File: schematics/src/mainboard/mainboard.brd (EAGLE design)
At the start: 58.4 x 99.1 mm, 65 parts, among them IC1 LM324N, IC2 7805T, IC3 UA741P, IC6 LM324N, IC8 CA3080E, Q1 BC550C, Q2 BC550C, Q3 BC550C

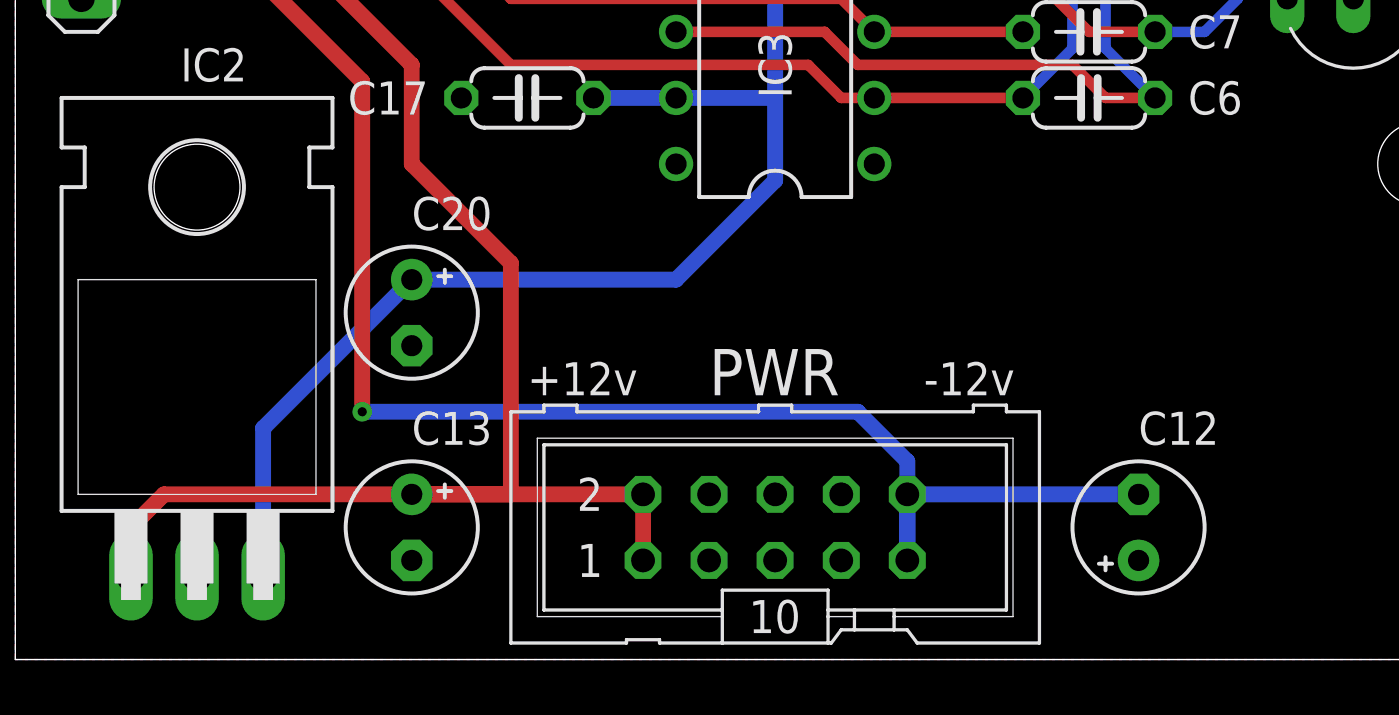
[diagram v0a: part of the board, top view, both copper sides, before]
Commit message: Updated Schematics, Fixed Power Socket orientation
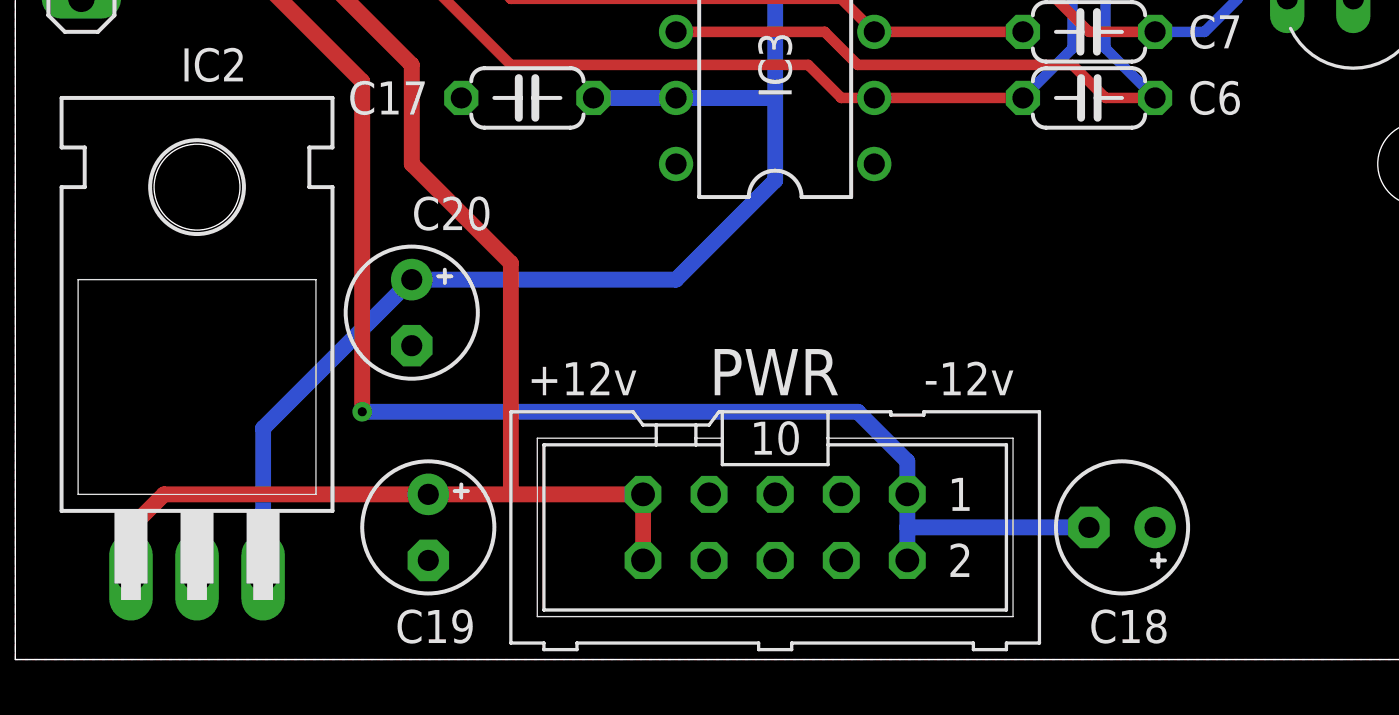
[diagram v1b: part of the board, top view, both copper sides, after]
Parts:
- removed C12, C13: 10uf, resistor:E2,5-5
- added C18, C19: 10uf, resistor:E2,5-5
- turned PWR to 180 degrees
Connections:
- net +12V: now also C19.+, PWR.10, PWR.9; no longer C13.+, PWR.1, PWR.2
- net -12V: now also C18.-, PWR.1, PWR.2; no longer C12.-, PWR.10, PWR.9
- net GND: now also C18.+, C19.-; no longer C12.+, C13.-
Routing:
- net -12V: track 62.8 -> 58.4 mm
- net +12V: track 62.4 -> 58.6 mm

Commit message: Fixed some bugs and updated documentation
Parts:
- C8: value 47nF/16v -> 47nF; device rcl:E2,5-6 -> rcl:C050-024X044
- R31: value 33k -> 22k
- R32: value 10k -> 100k
- moved IO_CON_2 0.63 mm to (56.5, 90.8)
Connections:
- net N$17: now also C8.2; no longer C8.-
- net N$18: now also C8.1; no longer C8.+
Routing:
- net N$18: track 42.4 -> 41.1 mm
- net N$17: track 34.8 -> 33.5 mm
- net PAN_B: track 36.2 -> 36.9 mm
- net PAN_A: track 33.6 -> 34.2 mm
- net SPEED_B: track 49.9 -> 50.6 mm
- net SPEED_A: track 23.4 -> 24.0 mm
- net OUTPUT: track 19.5 -> 20.1 mm
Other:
- board size 58.4 x 99.1 mm -> 59.1 x 99.1 mm
- board text added: "Coron DrumSynth 8 Clone 2021 v1.1 GERBSTER.NL"
- board text removed: "Coron DrumSynth 8 Clone 2021 GERBSTER.NL"
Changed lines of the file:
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@@
 <board>
 <plain>
-<wire x1="0" y1="0" x2="58.42" y2="0" width="0" layer="20"/>
-<wire x1="58.42" y1="0" x2="58.42" y2="99.06" width="0" layer="20"/>
-<wire x1="58.42" y1="99.06" x2="0" y2="99.05" width="0" layer="20"/>
+<wire x1="0" y1="0" x2="59.055" y2="0" width="0" layer="20"/>
+<wire x1="59.055" y1="0" x2="59.055" y2="99.06" width="0" layer="20"/>
+<wire x1="59.055" y1="99.06" x2="0" y2="99.05" width="0" layer="20"/>
 <wire x1="0" y1="99.05" x2="0" y2="0" width="0" layer="20"/>
 <text x="19.685" y="10.16" size="1.27" layer="25" font="vector">+12v</text>
 <text x="34.925" y="10.16" size="1.27" layer="25" font="vector">-12v</text>
 <text x="6.35" y="52.07" size="1.27" layer="25" font="vector" rot="R90">Coron DrumSynth 8 Clone
-2021
+2021 v1.1
 GERBSTER.NL</text>
-<hole x="53.975" y="19.05" drill="3.2004"/>
+<hole x="54.61" y="19.05" drill="3.2004"/>
 <hole x="2.54" y="49.53" drill="3.2004"/>
 </plain>
@@
 </element>
 <element name="C6" library="rcl" library_urn="urn:adsk.eagle:library:334" package="C050-024X044" package3d_urn="urn:adsk.eagle:package:23643/1" value="10nF" x="41.275" y="24.13" smashed="yes" rot="R180">
-<attribute name="NAME" x="45.085" y="20.955" size="1.27" layer="25" font="vector"/>
+<attribute name="NAME" x="45.085" y="23.495" size="1.27" layer="25" font="vector"/>
 <attribute name="POPULARITY" value="33" x="17.145" y="59.69" size="1.778" layer="27" rot="R180" display="off"/>
 <attribute name="SPICEPREFIX" value="C" x="17.145" y="59.69" size="1.778" layer="27" rot="R180" display="off"/>
@@
 </element>
 <element name="C7" library="rcl" library_urn="urn:adsk.eagle:library:334" package="C050-024X044" package3d_urn="urn:adsk.eagle:package:23643/1" value="22pF" x="41.275" y="21.59" smashed="yes">
-<attribute name="NAME" x="45.085" y="23.495" size="1.27" layer="25" font="vector"/>
+<attribute name="NAME" x="45.085" y="20.955" size="1.27" layer="25" font="vector"/>
 <attribute name="POPULARITY" value="33" x="73.025" y="-13.97" size="1.778" layer="27" display="off"/>
 <attribute name="SPICEPREFIX" value="C" x="73.025" y="-13.97" size="1.778" layer="27" display="off"/>
 <attribute name="VALUE" x="38.1" y="22.225" size="1.27" layer="27" font="vector" ratio="15" rot="R180"/>
 </element>
-<element name="C8" library="rcl" library_urn="urn:adsk.eagle:library:334" package="E2,5-6" package3d_urn="urn:adsk.eagle:package:23349/1" value="47nF/16v" x="50.8" y="41.275" smashed="yes" rot="R90">
+<element name="C8" library="rcl" library_urn="urn:adsk.eagle:library:334" package="C050-024X044" package3d_urn="urn:adsk.eagle:package:23643/1" value="47nF" x="50.8" y="41.275" smashed="yes" rot="R90">
 <attribute name="NAME" x="53.34" y="38.1" size="1.27" layer="25" font="vector"/>
-<attribute name="POPULARITY" value="14" x="78.74" y="79.375" size="1.778" layer="27" rot="R90" display="off"/>
+<attribute name="POPULARITY" value="33" x="78.74" y="79.375" size="1.778" layer="27" rot="R90" display="off"/>
 <attribute name="SPICEPREFIX" value="C" x="78.74" y="79.375" size="1.778" layer="27" rot="R90" display="off"/>
 <attribute name="VALUE" x="48.387" y="36.703" size="1.27" layer="27" font="vector" ratio="15"/>
@@
 <attribute name="VALUE" x="14.605" y="48.895" size="1.27" layer="27" font="vector" ratio="15"/>
 </element>
-<element name="R31" library="rcl" library_urn="urn:adsk.eagle:library:334" package="0207/7" package3d_urn="urn:adsk.eagle:package:23493/2" value="33k" x="41.275" y="89.535" smashed="yes" rot="R180">
+<element name="R31" library="rcl" library_urn="urn:adsk.eagle:library:334" package="0207/7" package3d_urn="urn:adsk.eagle:package:23493/2" value="22k" x="41.275" y="89.535" smashed="yes" rot="R180">
 <attribute name="NAME" x="38.735" y="88.9" size="1.27" layer="25" font="vector"/>
 <attribute name="POPULARITY" value="22" x="-27.305" y="163.195" size="1.778" layer="27" rot="R180" display="off"/>
@@
 <attribute name="VALUE" x="38.735" y="88.9" size="1.27" layer="27" font="vector" ratio="15"/>
 </element>
-<element name="R32" library="rcl" library_urn="urn:adsk.eagle:library:334" package="0207/7" package3d_urn="urn:adsk.eagle:package:23493/2" value="10k" x="41.275" y="84.455" smashed="yes" rot="R180">
+<element name="R32" library="rcl" library_urn="urn:adsk.eagle:library:334" package="0207/7" package3d_urn="urn:adsk.eagle:package:23493/2" value="100k" x="41.275" y="84.455" smashed="yes" rot="R180">
 <attribute name="NAME" x="43.815" y="85.09" size="1.27" layer="25" font="vector" rot="R180"/>
 <attribute name="POPULARITY" value="22" x="23.495" y="163.195" size="1.778" layer="27" rot="R180" display="off"/>
@@
 <attribute name="VALUE" x="18.415" y="12.7" size="1.27" layer="27" font="vector" ratio="15"/>
 </element>
-<element name="IO_CON_2" library="pinhead" library_urn="urn:adsk.eagle:library:325" package="1X06" package3d_urn="urn:adsk.eagle:package:22472/2" value="" x="55.88" y="90.805" smashed="yes" rot="R90">
-<attribute name="NAME" x="53.975" y="83.185" size="1.27" layer="25" font="vector" ratio="10" rot="R90"/>
-<attribute name="POPULARITY" value="79" x="55.88" y="90.805" size="1.778" layer="27" rot="R90" display="off"/>
-<attribute name="VALUE" x="59.055" y="83.185" size="1.27" layer="27" rot="R90"/>
+<element name="IO_CON_2" library="pinhead" library_urn="urn:adsk.eagle:library:325" package="1X06" package3d_urn="urn:adsk.eagle:package:22472/2" value="" x="56.515" y="90.805" smashed="yes" rot="R90">
+<attribute name="NAME" x="54.61" y="83.185" size="1.27" layer="25" font="vector" ratio="10" rot="R90"/>
+<attribute name="POPULARITY" value="79" x="56.515" y="90.805" size="1.778" layer="27" rot="R90" display="off"/>
+<attribute name="VALUE" x="59.69" y="83.185" size="1.27" layer="27" rot="R90"/>
 </element>
 <element name="PWR" library="con-ml" package="ML10" value="" x="29.21" y="5.08" smashed="yes" rot="R180">
@@
 <vertex x="0" y="0"/>
 <vertex x="0" y="99.06"/>
-<vertex x="58.42" y="99.06"/>
-<vertex x="58.42" y="0"/>
+<vertex x="59.055" y="99.06"/>
+<vertex x="59.055" y="0"/>
 </polygon>
 <polygon width="0.4064" layer="16">
 <vertex x="0" y="0"/>
-<vertex x="58.42" y="0"/>
-<vertex x="58.42" y="99.06"/>
+<vertex x="59.055" y="0"/>
+<vertex x="59.055" y="99.06"/>
 <vertex x="0" y="99.06"/>
 </polygon>
@@
 <wire x1="37.465" y1="92.075" x2="36.195" y2="90.805" width="0.4064" layer="1"/>
 <contactref element="IO_CON_2" pad="4"/>
-<wire x1="55.88" y1="92.075" x2="37.465" y2="92.075" width="0.4064" layer="1"/>
+<wire x1="56.515" y1="92.075" x2="37.465" y2="92.075" width="0.4064" layer="1"/>
 </signal>
 <signal name="SPEED_B">
@@
 <via x="27.94" y="88.265" extent="1-16" drill="0.35"/>
 <contactref element="IO_CON_2" pad="3"/>
-<wire x1="55.88" y1="89.535" x2="51.435" y2="89.535" width="0.4064" layer="1"/>
+<wire x1="56.515" y1="89.535" x2="51.435" y2="89.535" width="0.4064" layer="1"/>
 </signal>
 <signal name="N$6">
@@
 <contactref element="IC3" pad="6"/>
 <contactref element="R17" pad="1"/>
-<contactref element="C8" pad="+"/>
+<contactref element="C8" pad="1"/>
 <wire x1="25.4" y1="24.13" x2="31.115" y2="24.13" width="0.4064" layer="1"/>
 <wire x1="31.115" y1="24.13" x2="32.385" y2="22.86" width="0.4064" layer="1"/>
@@
 <wire x1="40.64" y1="22.86" x2="41.91" y2="21.59" width="0.4064" layer="1"/>
 <wire x1="41.91" y1="21.59" x2="43.815" y2="21.59" width="0.4064" layer="1"/>
-<wire x1="50.8" y1="40.005" x2="50.8" y2="38.1" width="0.4064" layer="16"/>
+<wire x1="50.8" y1="38.735" x2="50.8" y2="38.1" width="0.4064" layer="16"/>
 <wire x1="43.815" y1="21.59" x2="41.91" y2="23.495" width="0.4064" layer="16"/>
 <wire x1="41.91" y1="23.495" x2="41.91" y2="26.035" width="0.4064" layer="16"/>
@@
 </signal>
 <signal name="N$17">
-<contactref element="C8" pad="-"/>
+<contactref element="C8" pad="2"/>
 <contactref element="R18" pad="2"/>
 <wire x1="45.085" y1="74.93" x2="48.26" y2="71.755" width="0.4064" layer="16"/>
 <wire x1="48.26" y1="53.34" x2="50.8" y2="50.8" width="0.4064" layer="16"/>
-<wire x1="50.8" y1="50.8" x2="50.8" y2="42.545" width="0.4064" layer="16"/>
+<wire x1="50.8" y1="50.8" x2="50.8" y2="43.815" width="0.4064" layer="16"/>
 <wire x1="48.26" y1="71.755" x2="48.26" y2="53.34" width="0.4064" layer="16"/>
 </signal>
@@
 <via x="41.91" y="74.93" extent="1-16" drill="0.35"/>
 <contactref element="IO_CON_2" pad="5"/>
-<wire x1="55.88" y1="94.615" x2="45.085" y2="94.615" width="0.4064" layer="1"/>
+<wire x1="56.515" y1="94.615" x2="45.085" y2="94.615" width="0.4064" layer="1"/>
 </signal>
 <signal name="PAN_A">
@@
 <via x="50.8" y="81.915" extent="1-16" drill="0.35"/>
 <contactref element="IO_CON_2" pad="6"/>
-<wire x1="52.705" y1="97.155" x2="55.88" y2="97.155" width="0.4064" layer="16"/>
+<wire x1="52.705" y1="97.155" x2="56.515" y2="97.155" width="0.4064" layer="16"/>
 </signal>
 <signal name="N$31">
@@
 <wire x1="38.735" y1="86.995" x2="40.005" y2="85.725" width="0.4064" layer="1"/>
 <contactref element="IO_CON_2" pad="2"/>
-<wire x1="55.88" y1="86.995" x2="51.435" y2="86.995" width="0.4064" layer="1"/>
+<wire x1="56.515" y1="86.995" x2="51.435" y2="86.995" width="0.4064" layer="1"/>
 </signal>
 <signal name="TRIGGER">
@@
 <wire x1="47.625" y1="65.405" x2="48.895" y2="64.135" width="0.4064" layer="1"/>
 <wire x1="48.895" y1="64.135" x2="52.705" y2="64.135" width="0.4064" layer="1"/>
-<wire x1="52.705" y1="64.135" x2="55.88" y2="67.31" width="0.4064" layer="1"/>
-<wire x1="55.88" y1="67.31" x2="55.88" y2="84.455" width="0.4064" layer="1"/>
+<wire x1="52.705" y1="64.135" x2="56.515" y2="67.945" width="0.4064" layer="1"/>
+<wire x1="56.515" y1="67.945" x2="56.515" y2="84.455" width="0.4064" layer="1"/>
 </signal>
 </signals>
